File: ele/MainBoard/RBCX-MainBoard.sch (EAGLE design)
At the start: 318 parts, among them IC1 AMS1117-3.3, IC10 INA180A4, IC11 INA180A4, IC12 STM32F103VCT6, IC2 DRV8833PWP, IC3 INA180A4, IC4 INA180A4, IC5 DRV8833PWP, IC6 INA180A4, IC7 INA180A4, IC8 INA180A4, IC9 INA180A4, M1 DISPLAY-OLED-128X32, Q1 NCE20P45Q, Q10 2N7002, Q11 2N7002, Q2 NCE20P45Q, Q3 2N7002, Q4 2N7002, Q5 2N7002, Q6 2N7002, Q7 2N7002, Q8 2N7002, Q9 2N7002, X1 POWER_OUT, X2 POWER_IN, X3 52559-3092, X4 52559-2092, X5 uUSB, X6 M1, X7 M2, X8 M3, X9 M4, Y1 5032/2P, Y2 3215_2P

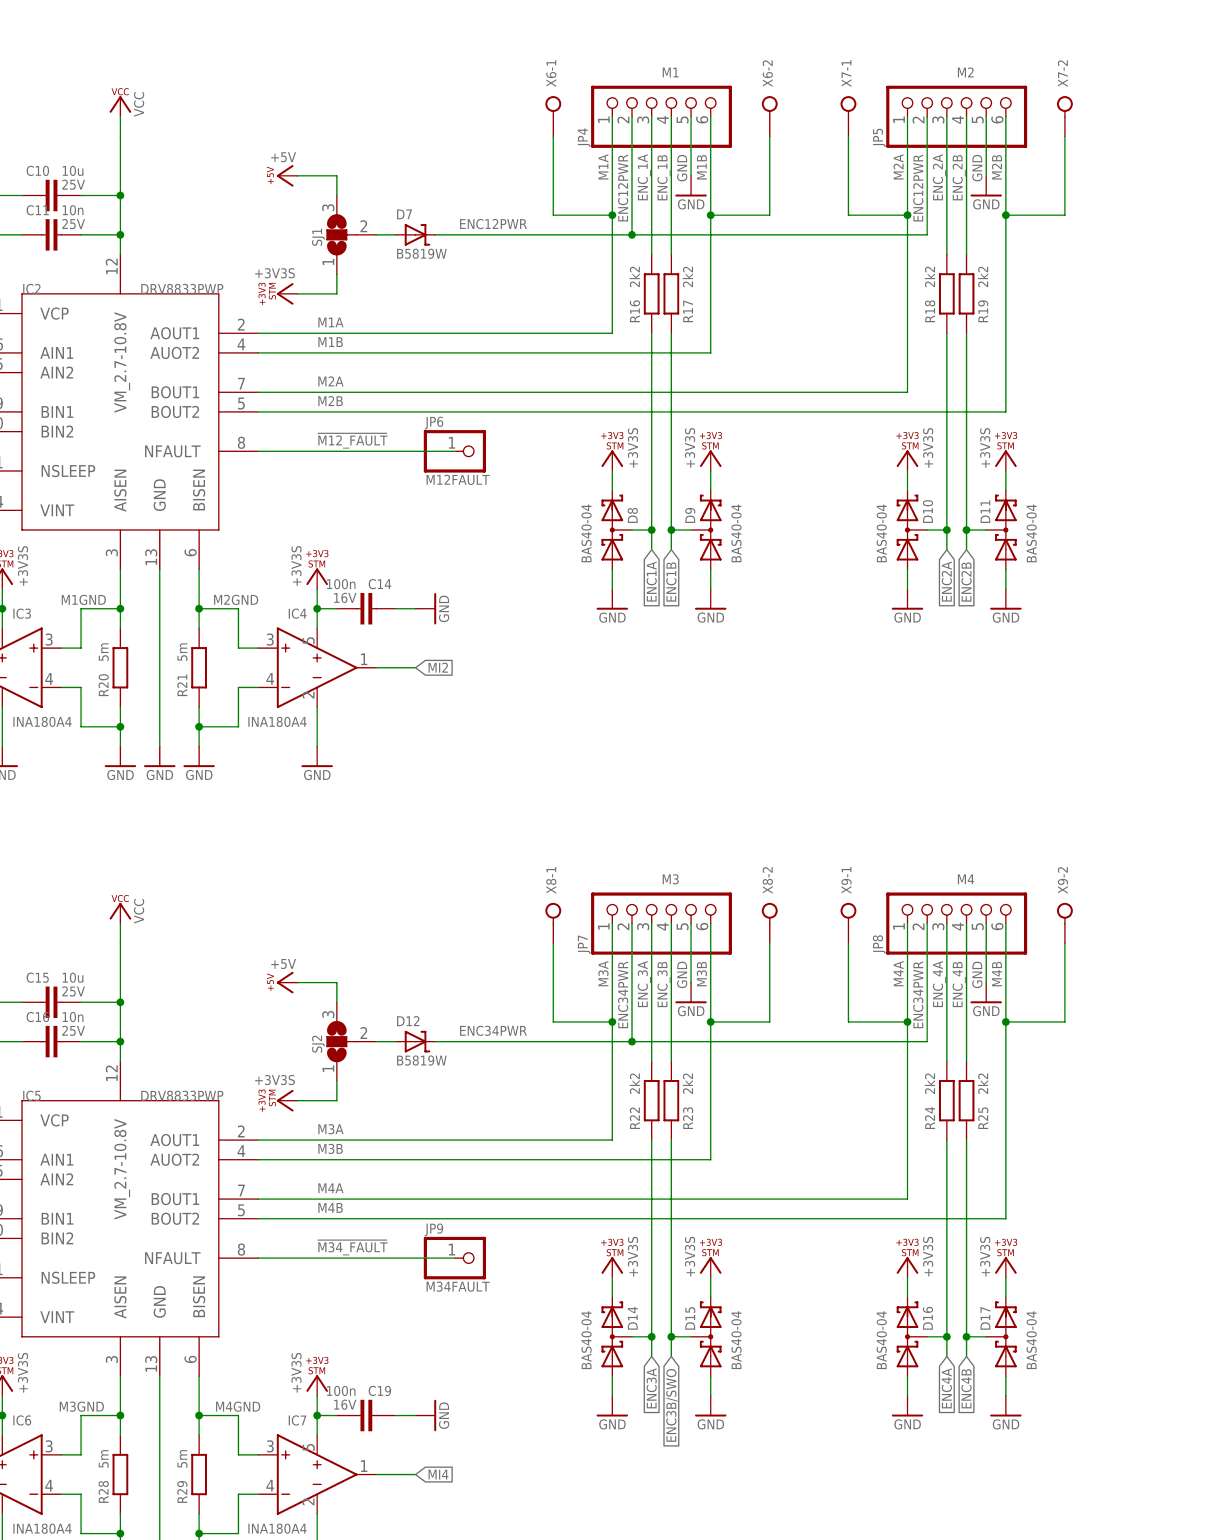
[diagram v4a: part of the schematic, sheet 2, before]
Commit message: MainBoard: 4 layers, motors connector, DRV8833, libraries
- set 4 layers stack + change DRC setting about same signals, the rest is still same (possible place
for improvements due to 4 layers stack and https://jlcpcb.com/capabilities/Capabilities)
- motors connectors - remove terminal blocks, replace pinheads with JST-PH6 (2mm x 6 pins)
- DRV8833
  - improve `DRV8833.lbr` library - fix thermal GND pad under the package
  - reroute on DPS and add thermal VIAs according http://www.ti.com/lit/an/slma004b/slma004b.pdf
- reroute `Q1` and `Q2` + main power terminal block
- libraries - add `jst-ph.lbr` and document `LIBRARIES.md` with source info about used libraries
  - please extend the `LIBRARIES.md` in the feature
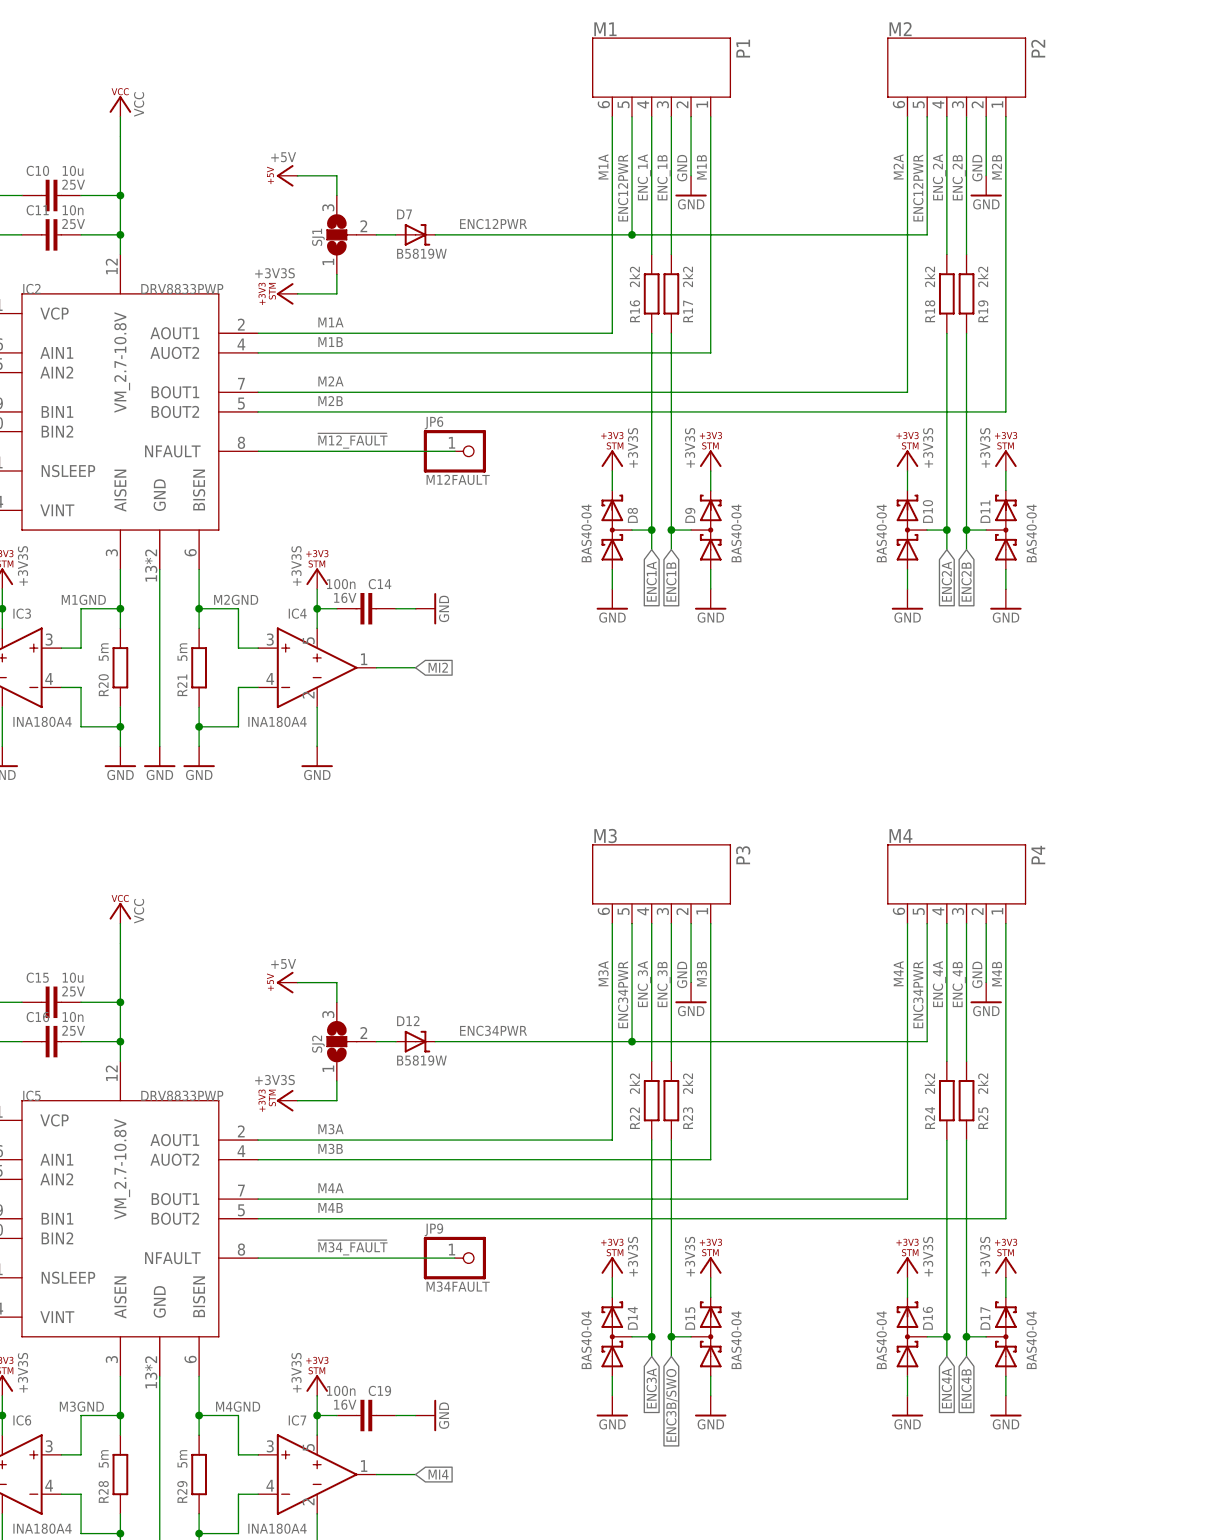
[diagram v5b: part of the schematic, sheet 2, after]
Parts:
- removed JP4: M1, pinhead:PINHD-1X6
- removed JP5: M2, pinhead:PINHD-1X6
- removed JP7: M3, pinhead:PINHD-1X6
- removed JP8: M4, pinhead:PINHD-1X6
- removed X6: M1, con-wago-508:W237-02P
- removed X7: M2, con-wago-508:W237-02P
- removed X8: M3, con-wago-508:W237-02P
- removed X9: M4, con-wago-508:W237-02P
- added P1: M1, jst-ph:JST-PH6
- added P2: M2, jst-ph:JST-PH6
- added P3: M3, jst-ph:JST-PH6
- added P4: M4, jst-ph:JST-PH6
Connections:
- net BAT+: now also X2-1.KL; no longer X2-2.KL
- net ENC12PWR: now also P1.5, P2.5; no longer JP4.2, JP5.2
- net ENC34PWR: now also P3.5, P4.5; no longer JP7.2, JP8.2
- net ENC_1A: now also P1.4; no longer JP4.3
- net ENC_1B: now also P1.3; no longer JP4.4
- net ENC_2A: now also P2.4; no longer JP5.3
- net ENC_2B: now also P2.3; no longer JP5.4
- net ENC_3A: now also P3.4; no longer JP7.3
- net ENC_3B: now also P3.3; no longer JP7.4
- net ENC_4A: now also P4.4; no longer JP8.3
- net ENC_4B: now also P4.3; no longer JP8.4
- net GND: now also P1.2, P2.2, P3.2, P4.2, X1-1.KL, X2-2.KL; no longer JP4.5, JP5.5, JP7.5, JP8.5, X1-2.KL, X2-1.KL
- net M1A: now also P1.6; no longer JP4.1, X6-1.KL
- net M1B: now also P1.1; no longer JP4.6, X6-2.KL
- net M2A: now also P2.6; no longer JP5.1, X7-1.KL
- net M2B: now also P2.1; no longer JP5.6, X7-2.KL
- net M3A: now also P3.6; no longer JP7.1, X8-1.KL
- net M3B: now also P3.1; no longer JP7.6, X8-2.KL
- net M4A: now also P4.6; no longer JP8.1, X9-1.KL
- net M4B: now also P4.1; no longer JP8.6, X9-2.KL
- net VCC: now also X1-2.KL; no longer X1-1.KL
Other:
- moved on the sheet: IC2, IC5, X1-1, X1-2, X2-1, X2-2

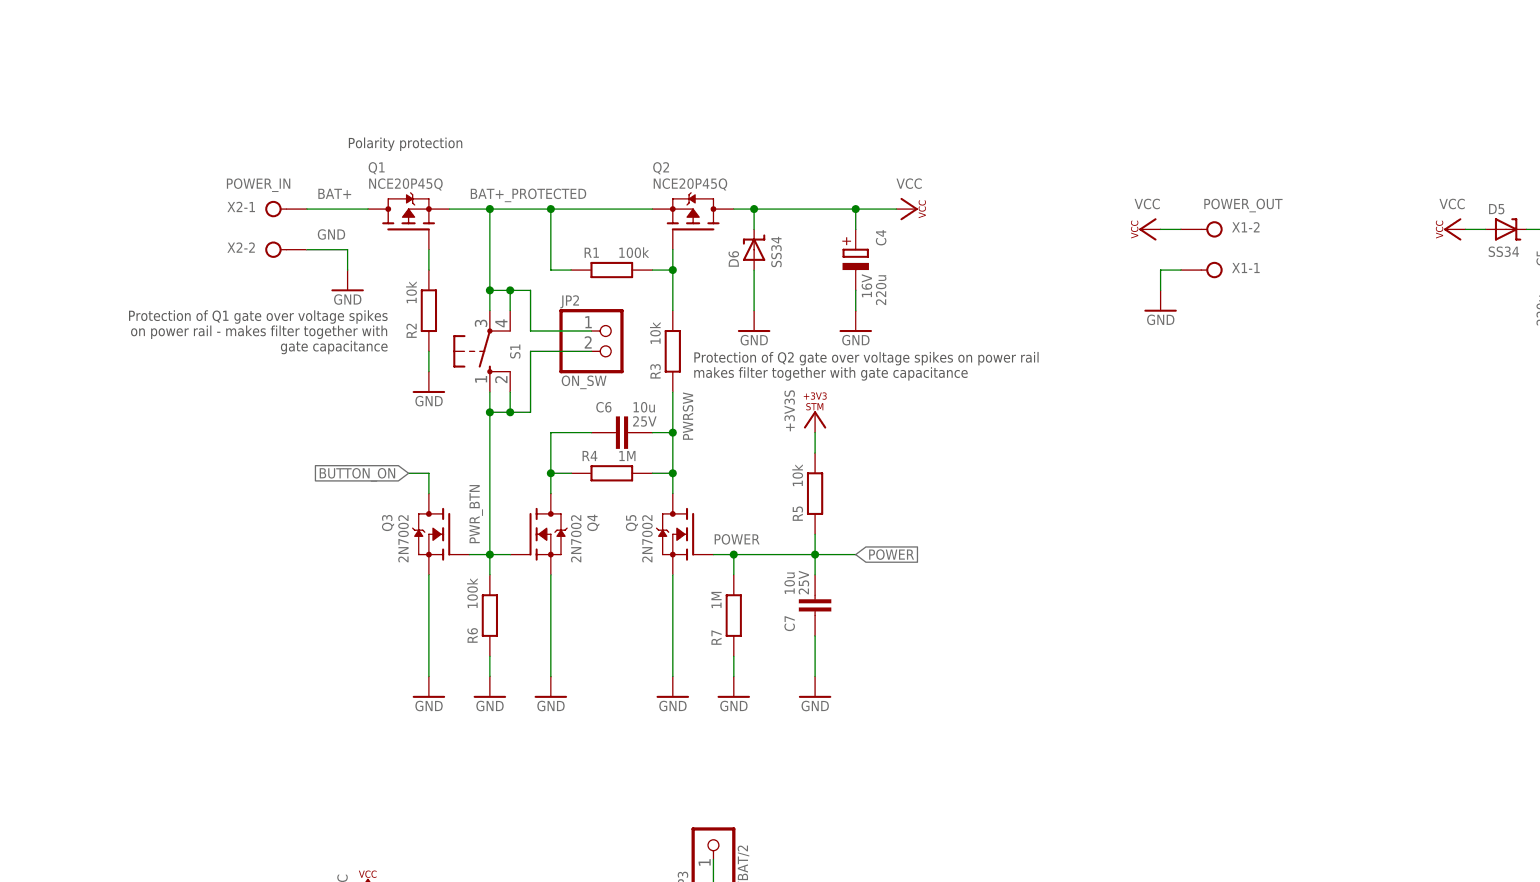
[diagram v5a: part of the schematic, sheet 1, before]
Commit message: MainBoard: Change power circuit to make ON button connected to GND
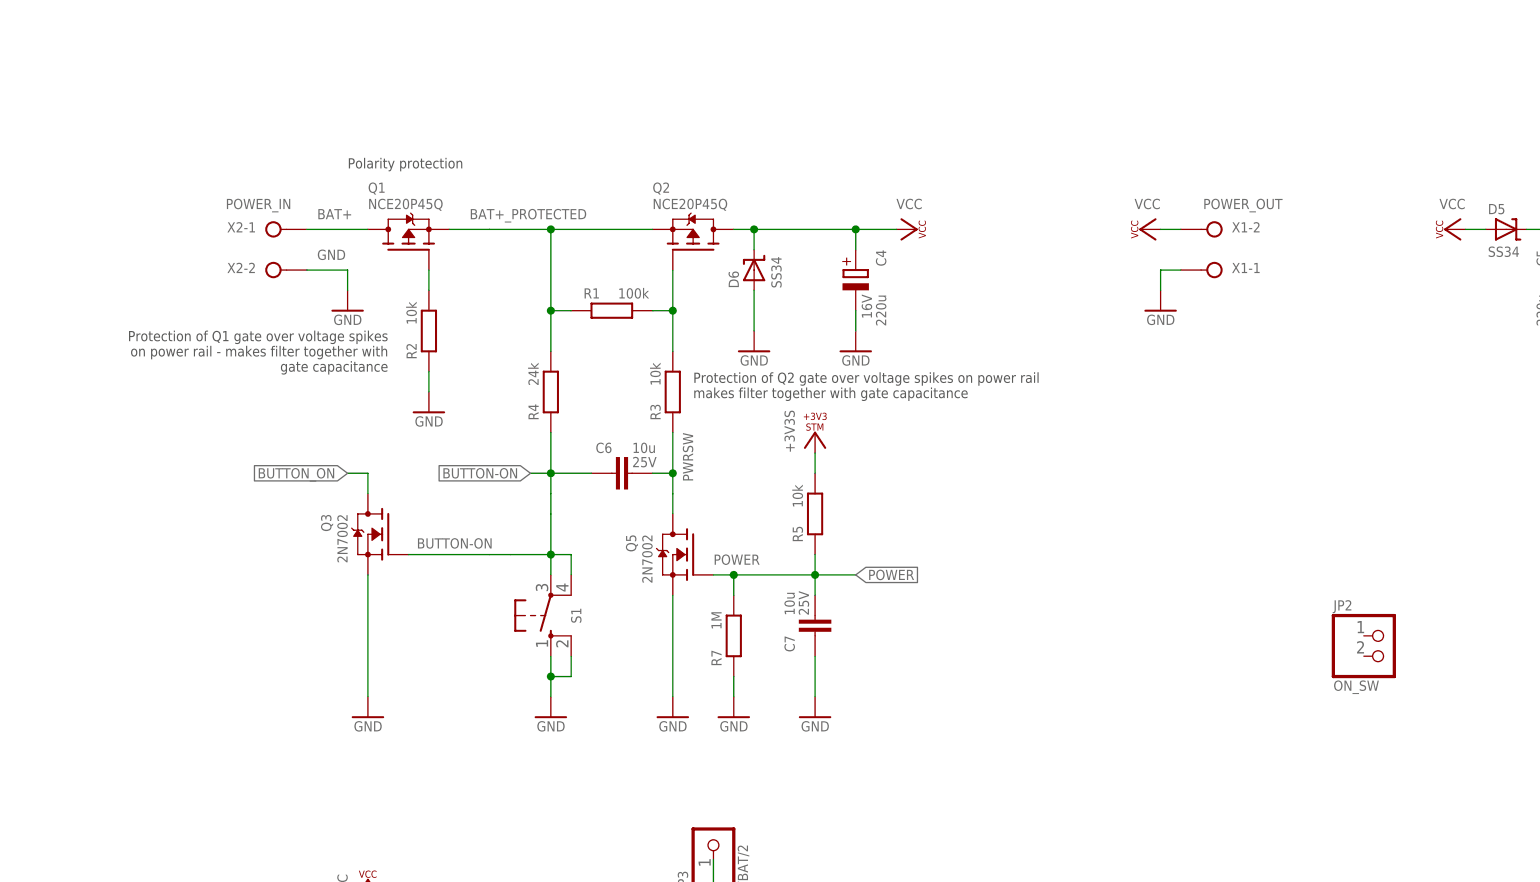
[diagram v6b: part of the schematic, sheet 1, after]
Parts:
- removed Q4: 2N7002, transistors:N-MOSFET-SOT23-GSD
- removed R6: 100k, rcl_upravena:R-EU_R0402
- JP20: device pinhead:PINHD-2X5 -> pinhead:PINHD-2X6
- R4: value 1M -> 24k
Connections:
- removed net N$11: C6.2, Q4.D, R4.1
- new net BUTTON-ON: C6.2, JP20.11, Q3.G, R4.1, S1.P, S1.P1
- net BAT+_PROTECTED: now also R4.2; no longer JP2.1, S1.P, S1.P1
- net GND: now also JP20.12, S1.S, S1.S1; no longer Q4.S, R6.1
- net PWRSW: no longer R4.2
- net PWR_BTN: no longer JP2.2, Q3.G, Q4.G, R6.2, S1.S, S1.S1
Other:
- moved on the sheet: C4, C6, C7, D6, JP2, Q1, Q2, Q3, Q5, R1, R2, R3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
